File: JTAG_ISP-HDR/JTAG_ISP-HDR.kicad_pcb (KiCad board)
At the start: 2 copper layers, 23.1 x 45.1 mm, 4 parts, among them J1 Conn_01x08, J2 Conn_01x08

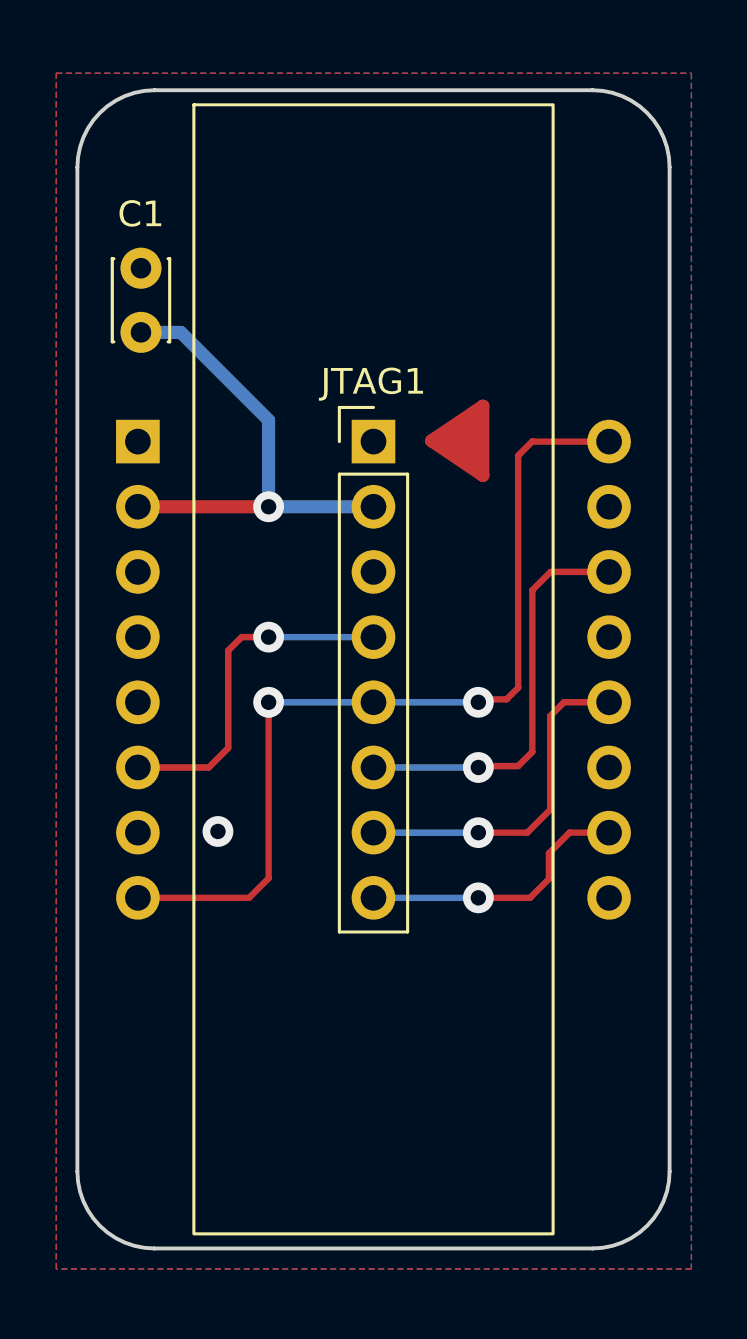
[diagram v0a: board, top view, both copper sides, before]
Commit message: + Ajout d'un trou sur chacun des 2 PCB pour pouvoir y fixer une dragone. + Ajout d'un espace de texte contenant mon nom et la date sur le PCB ISP. + Ajout d'un dossier contenant les fichiers générés pour panélisation par une application externe à KiCad. **Le circuit pour l'étage ISP est à vérifier**
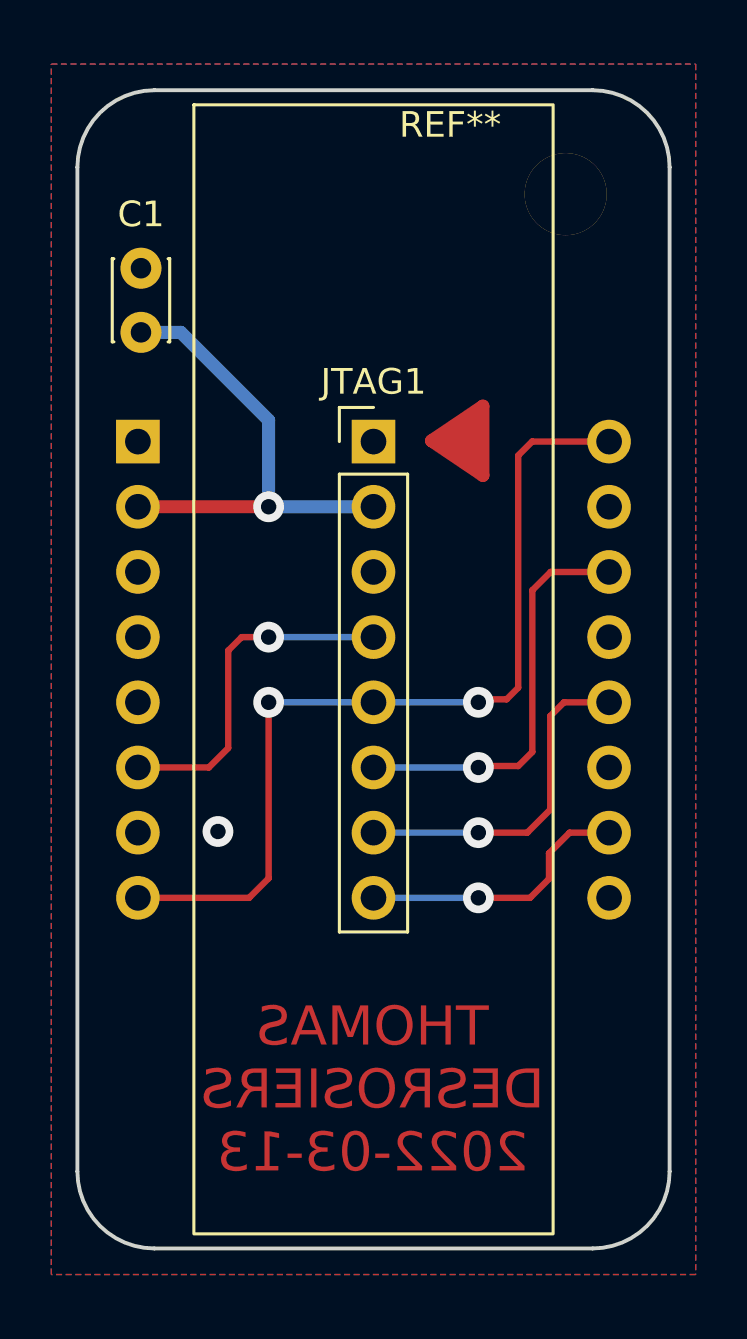
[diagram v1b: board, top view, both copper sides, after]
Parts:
- added REF**: MountingHole_3.2mm_M3, MountingHole:MountingHole_3.2mm_M3, F.Cu at (163.8, 65.9)
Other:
- board text added: "THOMAS DESROSIERS 2022-03-13"
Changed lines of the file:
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@@
     )
     (pad_to_mask_clearance 0)
+    (aux_axis_origin 143.806012 60.797592)
+    (grid_origin 143.806012 60.797592)
     (pcbplotparams
       (layerselection 0x0001000_ffffffff)
@@
     )
   )
+  (footprint "MountingHole:MountingHole_3.2mm_M3" (layer "F.Cu")
+    (at 163.85 65.86358)
+    (descr "Mounting Hole 3.2mm, no annular, M3")
+    (tags "mounting hole 3.2mm no annular m3")
+    (attr exclude_from_pos_files exclude_from_bom)
+    (fp_text reference "REF**" (at -4.500012 -2.699989) (layer "F.SilkS")
+      (effects (font (size 1 1) (thickness 0.15)))
+    )
+    (fp_text value "MountingHole_3.2mm_M3" (at 0 4.2) (layer "F.Fab")
+      (effects (font (size 1 1) (thickness 0.15)))
+    )
+    (fp_text user "${REFERENCE}" (at -4.500012 -2.699989) (layer "F.Fab")
+      (effects (font (size 1 1) (thickness 0.15)))
+    )
+    (fp_circle (center 0 0) (end 3.2 0) (layer "Cmts.User") (width 0.15) (fill none))
+    (fp_circle (center 0 0) (end 3.45 0) (layer "F.CrtYd") (width 0.05) (fill none))
+    (pad "" thru_hole circle locked (at 0 0) (size 3.200001 3.200001) (drill 3.200001) (layers *.Cu *.Mask))
+  )
   (footprint "Connector_PinHeader_2.54mm:PinHeader_1x08_P2.54mm_Vertical" (layer "B.Cu")
     (at 165.542001 75.50576 180)
@@
   (gr_arc (start 167.9 103.95) (mid 167.02132 106.07132) (end 164.9 106.95) (layer "Edge.Cuts") (width 0.15))
   (gr_rect (start 167.9 61.81358) (end 144.822002 106.95) (layer "User.1") (width 1.016) (fill none))
-  (gr_rect (start 168.75 61.15) (end 144 107.75) (layer "User.2") (width 0.2) (fill none))
+  (gr_rect (start 143.806012 60.797592) (end 168.915994 107.966002) (layer "User.2") (width 0.15) (fill none))
   (gr_rect (start 167.9 61.81358) (end 144.822002 106.95) (layer "User.9") (width 0.15) (fill none))
+  (gr_text "THOMAS\nDESROSIERS\n2022-03-13" (at 156.325011 100.749989) (layer "F.Cu")
+    (effects (font (size 1.524 1.524) (thickness 0.1905)) (justify mirror))
+  )
   (segment (start 147.180001 78.04576) (end 152.27424 78.04576) (width 0.508) (layer "F.Cu") (net 1))
   (via (at 152.27424 78.04576) (size 1.2) (drill 0.6) (layers "F.Cu" "B.Cu") (net 1))
@@
     (polygon
       (pts
-        (xy 168.75 107.75)
-        (xy 144 107.75)
-        (xy 144 61.15)
-        (xy 168.75 61.15)
+        (xy 168.915994 107.966002)
+        (xy 143.806012 107.966002)
+        (xy 143.806012 60.797592)
+        (xy 168.915994 60.797592)
       )
     )

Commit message: # [PCB] ~ Modification du PCB pour le projet ISP en fonction des nouvelles connexions sur son schéma. + Ajout de trous aux 4 coins du PCB des 2 projets (ISP & HDR). ~ Augmentation de la taille du PCB des 2 projets en ajoutant 20mills en haut et en bas. ~ Diminution de l'espace de texte (nom et date).
# [SCHÉMA]
~ Modification du schéma pour le projet ISP basé sur le fil JTAG -> ISP déjà existant.
+ Ajout de texte sur le schéma des 2 projets indiquant le nom des broches sur les headers.
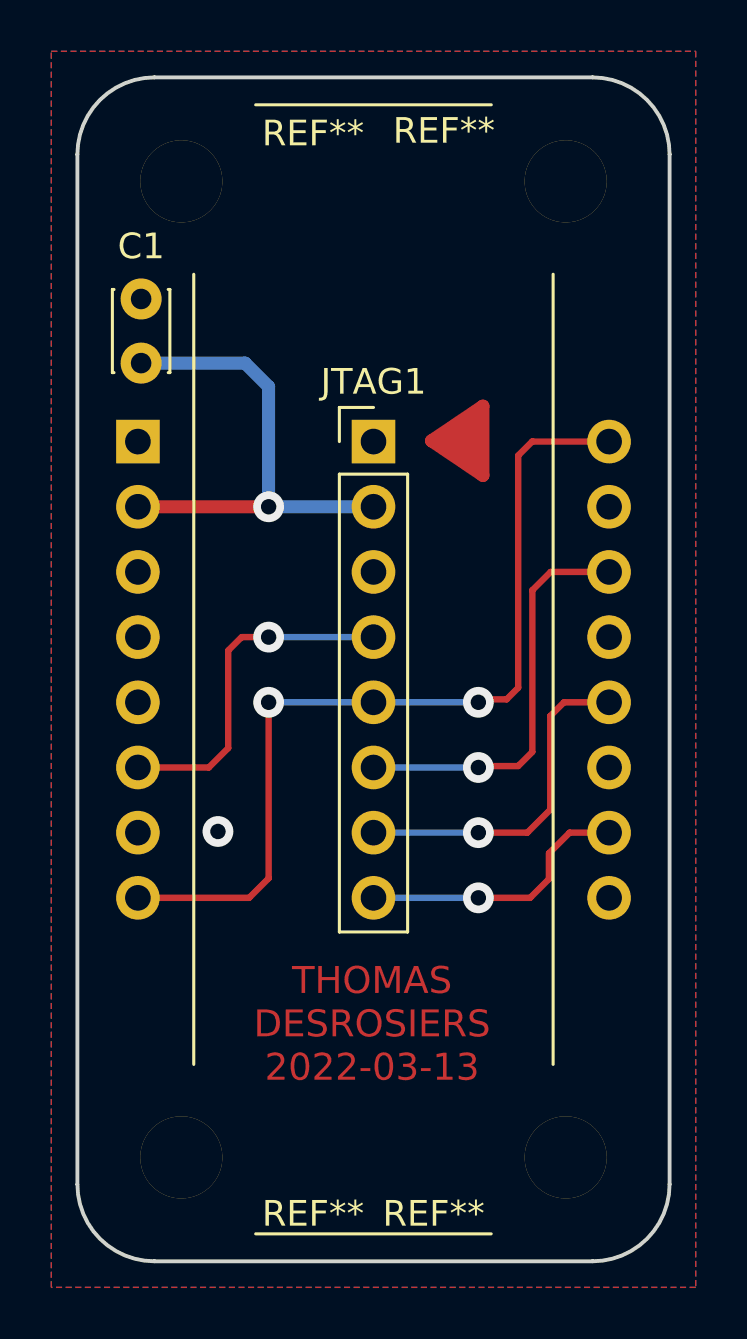
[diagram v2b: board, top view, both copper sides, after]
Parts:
- added REF**: MountingHole_3.2mm_M3, MountingHole:MountingHole_3.2mm_M3, F.Cu at (148.9, 65.4)
- added REF**: MountingHole_3.2mm_M3, MountingHole:MountingHole_3.2mm_M3, F.Cu at (163.8, 103.4)
- added REF**: MountingHole_3.2mm_M3, MountingHole:MountingHole_3.2mm_M3, F.Cu at (148.9, 103.4)
- moved C1 1.20 mm to (147.3, 72.4)
- moved REF** 0.50 mm to (163.8, 65.4)
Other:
- board size 23.1 x 45.1 mm -> 23.1 x 46.1 mm

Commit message: # [PCB] ~ Augmentation de la largeur des traces et du dégagement des traces à 20 mils.
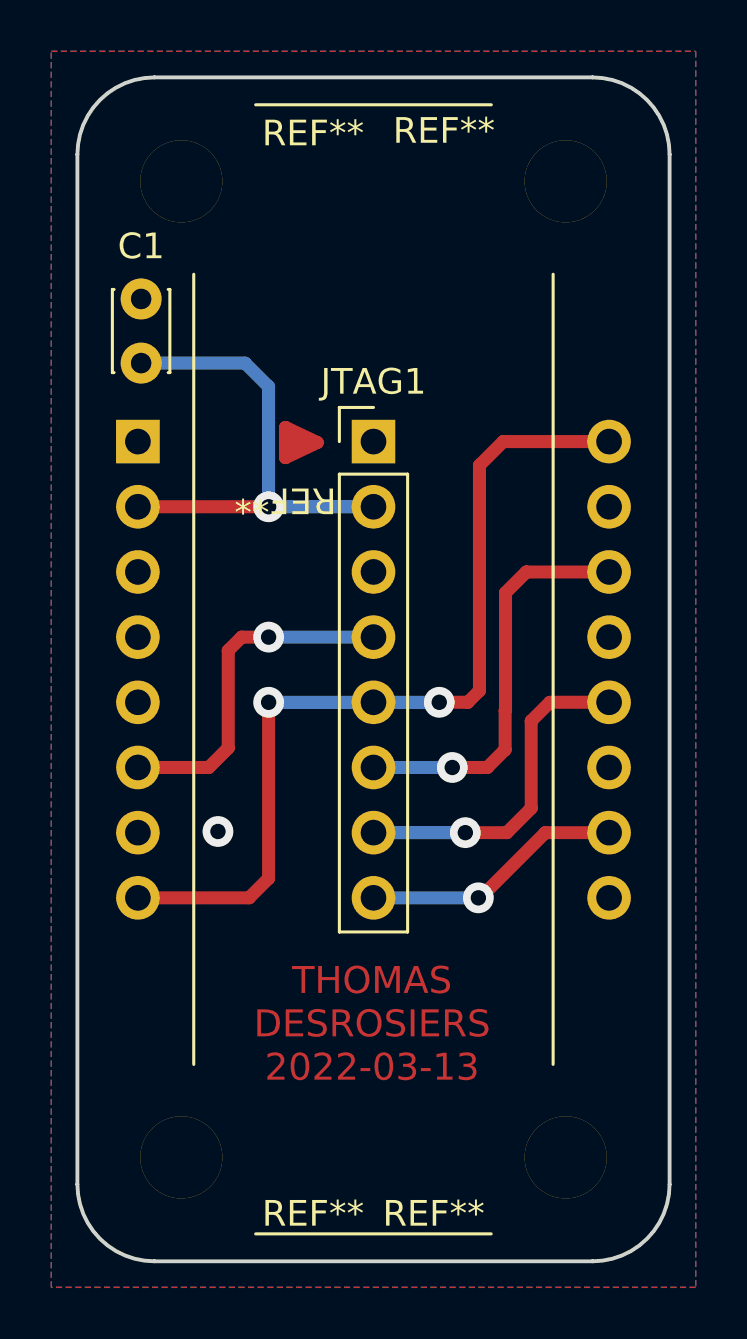
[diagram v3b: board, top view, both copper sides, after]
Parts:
- added REF**: Fleche_small, THOMAS_library:Fleche_small, F.Cu at (152.9, 75.9)
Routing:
- net Net-(J2-Pad5): track 13.4 -> 12.8 mm
- net Net-(J2-Pad7): track 10.8 -> 10.2 mm

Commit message: # [PCB] + Ajout d'un trou au bas du PCB pour le projet du projet HDR pour laisser passer la sur le PCB d'en dessous. - Suppression du texte (nom & date) sur le PCB du bas puisqu'il ne sera pas le plus visible.
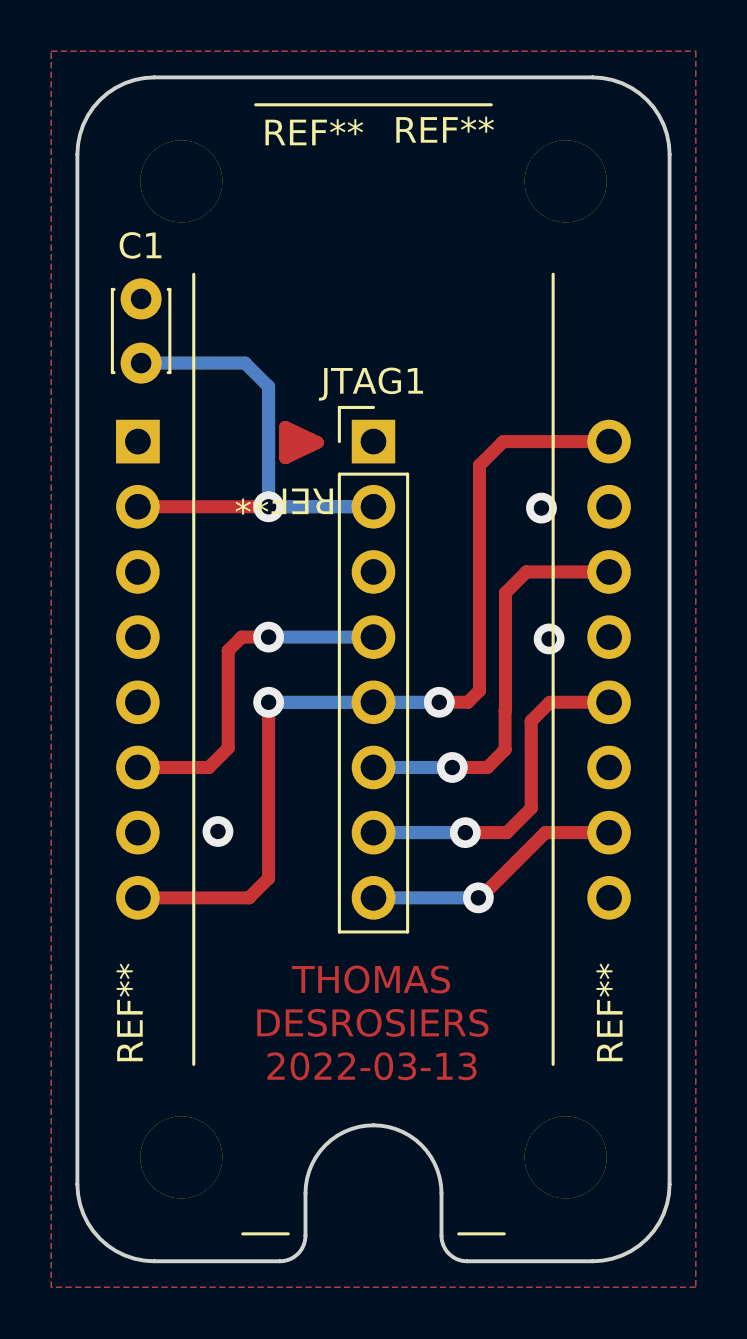
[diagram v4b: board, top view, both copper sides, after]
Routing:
- net GND: vias 1 -> 3
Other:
- outline, holes or cut-outs redrawn
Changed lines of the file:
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@@
     (tags "mounting hole 3.2mm no annular m3")
     (attr exclude_from_pos_files exclude_from_bom)
-    (fp_text reference "REF**" (at -5.143988 2.197568) (layer "F.SilkS")
+    (fp_text reference "REF**" (at 1.756012 -5.602432 270) (layer "F.SilkS")
       (effects (font (size 1 1) (thickness 0.15)))
     )
@@
       (effects (font (size 1 1) (thickness 0.15)))
     )
-    (fp_text user "${REFERENCE}" (at -5.143988 2.197568) (layer "F.Fab")
+    (fp_text user "${REFERENCE}" (at 1.756012 -5.602432 270) (layer "F.Fab")
       (effects (font (size 1 1) (thickness 0.15)))
     )
@@
     (tags "mounting hole 3.2mm no annular m3")
     (attr exclude_from_pos_files exclude_from_bom)
-    (fp_text reference "REF**" (at 5.13401 2.197568) (layer "F.SilkS")
+    (fp_text reference "REF**" (at -1.96599 -5.602432 90) (layer "F.SilkS")
       (effects (font (size 1 1) (thickness 0.15)))
     )
@@
       (effects (font (size 1 1) (thickness 0.15)))
     )
-    (fp_text user "${REFERENCE}" (at 5.13401 2.197568) (layer "F.Fab")
+    (fp_text user "${REFERENCE}" (at -1.96599 -5.602432 90) (layer "F.Fab")
       (effects (font (size 1 1) (thickness 0.15)))
     )
@@
   )
   (footprint "THOMAS_library:PicKit4-2" (layer "F.Cu")
-    (at 156.361001 75.50576)
+    (at 156.361003 75.505767)
     (descr "Through hole straight pin header, 1x08, 2.54mm pitch, single row")
     (tags "Through hole pin header THT 1x08 2.54mm single row")
@@
     (fp_line (start 4.591065 -13.125) (end -4.591065 -13.125) (layer "F.SilkS") (width 0.12))
     (fp_line (start -1.33 -1.33) (end 0 -1.33) (layer "F.SilkS") (width 0.12))
-    (fp_line (start 4.587001 30.874995) (end -4.591065 30.874995) (layer "F.SilkS") (width 0.12))
+    (fp_line (start 5.095001 30.874995) (end 3.321065 30.874995) (layer "F.SilkS") (width 0.12))
     (fp_line (start -7.004065 -6.521) (end -7.004065 24.270995) (layer "F.SilkS") (width 0.12))
     (fp_line (start -1.33 19.11) (end 1.33 19.11) (layer "F.SilkS") (width 0.12))
     (fp_line (start 1.33 1.27) (end 1.33 19.11) (layer "F.SilkS") (width 0.12))
     (fp_line (start -1.33 1.27) (end -1.33 19.11) (layer "F.SilkS") (width 0.12))
+    (fp_line (start -3.321065 30.874995) (end -5.095001 30.874995) (layer "F.SilkS") (width 0.12))
     (fp_line (start -1.33 0) (end -1.33 -1.33) (layer "F.SilkS") (width 0.12))
     (fp_line (start 7.000001 -6.521) (end 7.000001 24.270995) (layer "F.SilkS") (width 0.12))
@@
     )
   )
+  (gr_line (start 153.710992 104.800011) (end 153.710992 106.45) (layer "Edge.Cuts") (width 0.15))
   (gr_arc (start 167.9 104.45) (mid 167.02132 106.57132) (end 164.9 107.45) (layer "Edge.Cuts") (width 0.15))
-  (gr_line (start 147.822002 107.45) (end 164.9 107.45) (layer "Edge.Cuts") (width 0.15))
+  (gr_line (start 164.899997 107.45) (end 160.010981 107.45) (layer "Edge.Cuts") (width 0.15))
+  (gr_arc (start 153.710992 104.800011) (mid 154.487159 102.926178) (end 156.360992 102.150011) (layer "Edge.Cuts") (width 0.15))
   (gr_line (start 167.9 104.45) (end 167.9 64.31358) (layer "Edge.Cuts") (width 0.15))
   (gr_arc (start 144.822002 64.31358) (mid 145.700682 62.19226) (end 147.822002 61.31358) (layer "Edge.Cuts") (width 0.15))
   (gr_line (start 164.9 61.31358) (end 147.822002 61.31358) (layer "Edge.Cuts") (width 0.15))
+  (gr_arc (start 156.360981 102.150011) (mid 158.234814 102.926178) (end 159.010981 104.800011) (layer "Edge.Cuts") (width 0.15))
   (gr_arc (start 164.9 61.31358) (mid 167.02132 62.19226) (end 167.9 64.31358) (layer "Edge.Cuts") (width 0.15))
+  (gr_line (start 159.010981 106.45) (end 159.010981 104.800011) (layer "Edge.Cuts") (width 0.15))
+  (gr_line (start 152.710992 107.45) (end 147.822002 107.45) (layer "Edge.Cuts") (width 0.15))
+  (gr_arc (start 160.010981 107.45) (mid 159.303874 107.157107) (end 159.010981 106.45) (layer "Edge.Cuts") (width 0.15))
+  (gr_arc (start 153.710992 106.45) (mid 153.418099 107.157107) (end 152.710992 107.45) (layer "Edge.Cuts") (width 0.15))
   (gr_arc (start 147.822002 107.45) (mid 145.700682 106.57132) (end 144.822002 104.45) (layer "Edge.Cuts") (width 0.15))
   (gr_line (start 144.822002 64.31358) (end 144.822002 104.45) (layer "Edge.Cuts") (width 0.15))
   (gr_rect (start 167.899994 61.313568) (end 144.822012 107.450001) (layer "User.1") (width 1.016) (fill none))
   (gr_rect (start 143.806012 60.297568) (end 168.915994 108.466001) (layer "User.2") (width 0.15) (fill none))
+  (gr_line (start 147.822006 107.450001) (end 164.9 107.450001) (layer "User.8") (width 0.15))
   (gr_rect (start 167.9 61.31358) (end 144.822002 107.45) (layer "User.9") (width 0.15) (fill none))
   (gr_text "THOMAS\nDESROSIERS\n2022-03-13" (at 156.306012 98.197568) (layer "F.Cu")
@@
   (segment (start 152.27424 73.365796) (end 152.27424 78.04576) (width 0.508) (layer "B.Cu") (net 1))
   (via (at 150.3 90.7) (size 1.2) (drill 0.6) (layers "F.Cu" "B.Cu") (free) (net 2))
+  (via (at 162.906012 78.097568) (size 1.2) (drill 0.6) (layers "F.Cu" "B.Cu") (free) (net 2))
+  (via (at 163.206012 83.197568) (size 1.2) (drill 0.6) (layers "F.Cu" "B.Cu") (free) (net 2))
   (segment (start 150.7 87.45) (end 150.7 83.65) (width 0.508) (layer "F.Cu") (net 6))
   (segment (start 150.7 83.65) (end 151.22424 83.12576) (width 0.508) (layer "F.Cu") (net 6))
